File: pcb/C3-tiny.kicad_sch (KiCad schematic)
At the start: 29 parts, among them J1 USB_C_Receptacle_USB2.0, J2 Conn_01x10_Pin, J3 Conn_01x10_Pin, U1 ESP32-C3-MINI-1, U2 NCP692MN33T2G, U3 SHT31-DIS

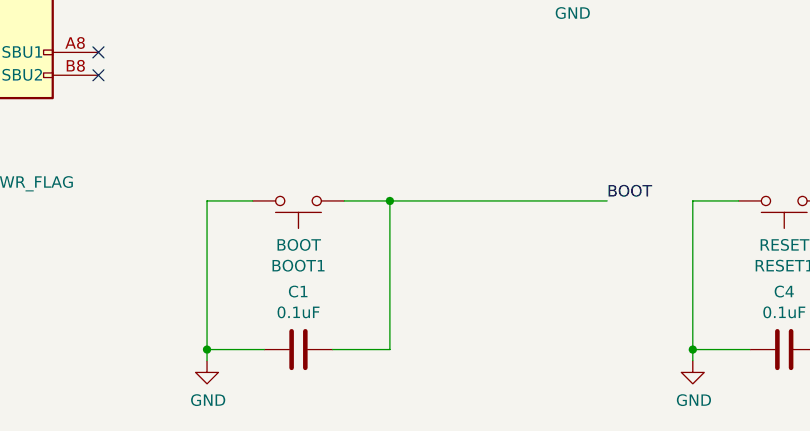
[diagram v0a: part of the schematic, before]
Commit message: Removed cap on BOOT. Cleanup some minor errors
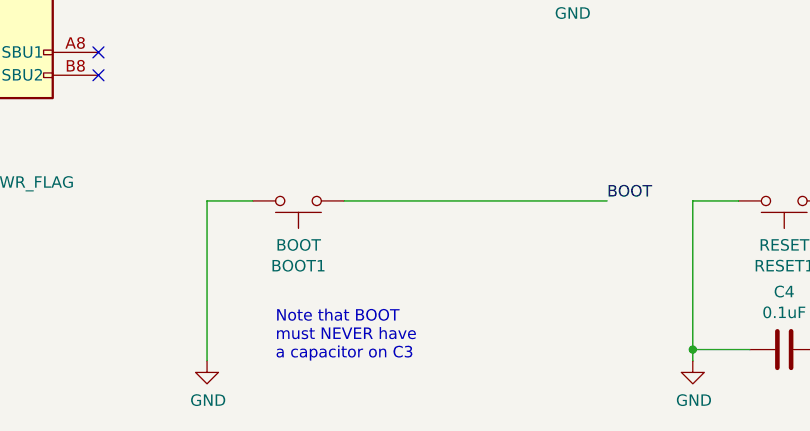
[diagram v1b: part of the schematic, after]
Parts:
- removed C1: 0.1uF, Capacitor_SMD:C_0603_1608Metric_Pad1.08x0.95mm_HandSolder, symbol Device:C
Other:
- note added: "Note that BOOT must NEVER have a capacitor on C3"
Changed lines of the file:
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@@
   (junction (at 97.79 127) (diameter 0) (color 0 0 0 0)
   )
-  (junction (at 77.47 171.45) (diameter 0) (color 0 0 0 0)
-  )
   (junction (at 29.845 168.91) (diameter 0) (color 0 0 0 0)
   )
@@
   )
   (junction (at 47.625 144.78) (diameter 0) (color 0 0 0 0)
-  )
-  (junction (at 57.15 187.96) (diameter 0) (color 0 0 0 0)
   )
   (junction (at 147.32 171.45) (diameter 0) (color 0 0 0 0)
@@
     (stroke (width 0) (type default))
   )
-  (wire (pts (xy 77.47 187.96) (xy 77.47 171.45))
-    (stroke (width 0) (type default))
-  )
   (wire (pts (xy 111.125 187.96) (xy 111.125 171.45))
     (stroke (width 0) (type default))
@@
     (stroke (width 0) (type default))
   )
-  (wire (pts (xy 71.12 187.96) (xy 77.47 187.96))
-    (stroke (width 0) (type default))
-  )
   (wire (pts (xy 227.33 49.53) (xy 240.03 49.53))
     (stroke (width 0) (type default))
@@
     (stroke (width 0) (type default))
   )
-  (wire (pts (xy 72.39 171.45) (xy 77.47 171.45))
-    (stroke (width 0) (type default))
-  )
-  (wire (pts (xy 57.15 187.96) (xy 57.15 189.23))
-    (stroke (width 0) (type default))
-  )
   (wire (pts (xy 111.125 171.45) (xy 116.205 171.45))
     (stroke (width 0) (type default))
@@
     (stroke (width 0) (type default))
   )
-  (wire (pts (xy 77.47 171.45) (xy 101.6 171.45))
+  (wire (pts (xy 72.39 171.45) (xy 101.6 171.45))
     (stroke (width 0) (type default))
   )
@@
     (stroke (width 0) (type default))
   )
-  (wire (pts (xy 63.5 187.96) (xy 57.15 187.96))
-    (stroke (width 0) (type default))
-  )
-  (wire (pts (xy 57.15 187.96) (xy 57.15 171.45))
+  (wire (pts (xy 57.15 171.45) (xy 57.15 189.23))
     (stroke (width 0) (type default))
   )
@@
   (wire (pts (xy 73.025 144.78) (xy 81.915 144.78))
     (stroke (width 0) (type default))
+  )
+  (text "Note that BOOT\nmust NEVER have\na capacitor on C3" (at 64.77 189.23 0)
+    (effects (font (size 1.27 1.27)) (justify left bottom))
   )
   (label "IO1" (at 273.05 36.83 180) (fields_autoplaced)
@@
         )
       )
-    )
-  )
-  (symbol (lib_id "Device:C") (at 67.31 187.96 270) (unit 1)
-    (in_bom yes) (on_board yes) (dnp no)
-    (property "Reference" "C1" (at 67.31 181.5592 90)
-      (effects (font (size 1.27 1.27)))
-    )
-    (property "Value" "0.1uF" (at 67.31 183.8706 90)
-      (effects (font (size 1.27 1.27)))
-    )
-    (property "Footprint" "Capacitor_SMD:C_0603_1608Metric_Pad1.08x0.95mm_HandSolder" (at 63.5 188.9252 0)
-      (effects (font (size 1.27 1.27)) hide)
-    )
-    (property "Datasheet" "~" (at 67.31 187.96 0)
-      (effects (font (size 1.27 1.27)) hide)
-    )
-    (pin "1")
-    (pin "2")
-    (instances
-      (project "C3-tiny"
-        (path "/0b366bfd-aac6-4fb7-a594-083941468da3"
-          (reference "C1") (unit 1)
-        )
-      )
-      (project "TastaturPcb"
-        (path "/4fca5230-0d35-4f80-99ad-7103e284e6f0"
-          (reference "C2") (unit 1)
-        )
-      )
